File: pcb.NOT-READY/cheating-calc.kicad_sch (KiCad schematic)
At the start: 22 parts, among them J1 Conn_01x04, J2 Conn_01x04, Q1 MMBF170, Q2 MMBF170, U1 ESP32-C3-MINI-1-N4, U2 AP7215-33YG-13, U3 TLV75533PDQNR, U4 TLV75533PDRVR

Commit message: update cap
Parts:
- removed C1, C2: CL21B105KBFNNNE, easyeda2kicad:C0805, symbol easyeda2kicad:CL21B105KBFNNNE
- added C1, C2: CL21B105KPFNNNE, easyeda2kicad:C0805, symbol easyeda2kicad:CL21B105KPFNNNE
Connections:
- net +3.3V: now also C2.1
- net +5V: now also C1.1
- net GND: now also C1.2, C2.2
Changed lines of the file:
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@@
-	)
-	(symbol
-		(lib_id "easyeda2kicad:CL21B105KBFNNNE")
-		(at 100.33 74.93 270)
-		(unit 1)
-		(exclude_from_sim no)
-		(in_bom yes)
-		(on_board yes)
-		(dnp no)
-		(property "Reference" "C1"
-			(at 96.774 74.93 0)
-			(effects
-				(font
-					(size 1.27 1.27)
-				)
-			)
-		)
-		(property "Value" "CL21B105KBFNNNE"
-			(at 104.14 74.93 0)
-			(effects
-				(font
-					(size 1.27 1.27)
-				)
-			)
-		)
-		(property "Footprint" "easyeda2kicad:C0805"
-			(at 92.71 74.93 0)
-			(effects
-				(font
-					(size 1.27 1.27)
-				)
-				(hide yes)
-			)
-		)
-		(property "Datasheet" "https://lcsc.com/product-detail/Multilayer-Ceramic-Capacitors-MLCC-SMD-SMT_SAMSUNG_CL21B105KBFNNNE_1uF-105-10-50V_C28323.html"
-			(at 90.17 74.93 0)
-			(effects
-				(font
-					(size 1.27 1.27)
-				)
-				(hide yes)
-			)
-		)
-		(property "Description" ""
-			(at 100.33 74.93 0)
-			(effects
-				(font
-					(size 1.27 1.27)
-				)
-				(hide yes)
-			)
-		)
-		(property "LCSC Part" "C28323"
-			(at 87.63 74.93 0)
-			(effects
-				(font
-					(size 1.27 1.27)
-				)
-				(hide yes)
-			)
-		)
-		(pin "2"
-		)
-		(pin "1"
-		)
-		(instances
-			(project "cheating-calc"
-				(path "/dc32c202-8f02-44ca-a16c-c11d7f3acb8d"
-					(reference "C1")
-					(unit 1)
-				)
-			)
-		)
 	)
 	(symbol
@@
 	)
 	(symbol
+		(lib_id "easyeda2kicad:CL21B105KPFNNNE")
+		(at 128.27 74.93 270)
+		(unit 1)
+		(exclude_from_sim no)
+		(in_bom yes)
+		(on_board yes)
+		(dnp no)
+		(property "Reference" "C2"
+			(at 123.19 74.93 90)
+			(effects
+				(font
+					(size 1.27 1.27)
+				)
+				(justify left)
+			)
+		)
+		(property "Value" "CL21B105KPFNNNE"
+			(at 130.302 74.93 90)
+			(effects
+				(font
+					(size 1.27 1.27)
+				)
+				(justify left)
+			)
+		)
+		(property "Footprint" "easyeda2kicad:C0805"
+			(at 120.65 74.93 0)
+			(effects
+				(font
+					(size 1.27 1.27)
+				)
+				(hide yes)
+			)
+		)
+		(property "Datasheet" "https://lcsc.com/product-detail/Multilayer-Ceramic-Capacitors-MLCC-SMD-SMT_SAMSUNG_CL21B105KPFNNNE_1uF-105-10-10V_C107367.html"
+			(at 118.11 74.93 0)
+			(effects
+				(font
+					(size 1.27 1.27)
+				)
+				(hide yes)
+			)
+		)
+		(property "Description" ""
+			(at 128.27 74.93 0)
+			(effects
+				(font
+					(size 1.27 1.27)
+				)
+				(hide yes)
+			)
+		)
+		(property "LCSC Part" "C107367"
+			(at 115.57 74.93 0)
+			(effects
+				(font
+					(size 1.27 1.27)
+				)
+				(hide yes)
+			)
+		)
+		(pin "1"
+		)
+		(pin "2"
+		)
+		(instances
+			(project "cheating-calc"
+				(path "/dc32c202-8f02-44ca-a16c-c11d7f3acb8d"
+					(reference "C2")
+					(unit 1)
+				)
+			)
+		)
+	)
+	(symbol
 		(lib_id "easyeda2kicad:0603WAF1002T5E")
 		(at 177.8 71.12 0)
@@
 	)
 	(symbol
+		(lib_id "easyeda2kicad:CL21B105KPFNNNE")
+		(at 100.33 74.93 90)
+		(mirror x)
+		(unit 1)
+		(exclude_from_sim no)
+		(in_bom yes)
+		(on_board yes)
+		(dnp no)
+		(property "Reference" "C1"
+			(at 105.41 74.93 90)
+			(effects
+				(font
+					(size 1.27 1.27)
+				)
+				(justify left)
+			)
+		)
+		(property "Value" "CL21B105KPFNNNE"
+			(at 98.298 74.93 90)
+			(effects
+				(font
+					(size 1.27 1.27)
+				)
+				(justify left)
+			)
+		)
+		(property "Footprint" "easyeda2kicad:C0805"
+			(at 107.95 74.93 0)
+			(effects
+				(font
+					(size 1.27 1.27)
+				)
+				(hide yes)
+			)
+		)
+		(property "Datasheet" "https://lcsc.com/product-detail/Multilayer-Ceramic-Capacitors-MLCC-SMD-SMT_SAMSUNG_CL21B105KPFNNNE_1uF-105-10-10V_C107367.html"
+			(at 110.49 74.93 0)
+			(effects
+				(font
+					(size 1.27 1.27)
+				)
+				(hide yes)
+			)
+		)
+		(property "Description" ""
+			(at 100.33 74.93 0)
+			(effects
+				(font
+					(size 1.27 1.27)
+				)
+				(hide yes)
+			)
+		)
+		(property "LCSC Part" "C107367"
+			(at 113.03 74.93 0)
+			(effects
+				(font
+					(size 1.27 1.27)
+				)
+				(hide yes)
+			)
+		)
+		(pin "1"
+		)
+		(pin "2"
+		)
+		(instances
+			(project ""
+				(path "/dc32c202-8f02-44ca-a16c-c11d7f3acb8d"
+					(reference "C1")
+					(unit 1)
+				)
+			)
+		)
+	)
+	(symbol
 		(lib_id "Jumper:SolderJumper_2_Open")
 		(at 166.37 68.58 0)
@@
 					(unit 1)
 				)
-			)
-		)
-	)
-	(symbol
-		(lib_id "easyeda2kicad:CL21B105KBFNNNE")
-		(at 128.27 74.93 270)
-		(unit 1)
-		(exclude_from_sim no)
-		(in_bom yes)
-		(on_board yes)
-		(dnp no)
-		(property "Reference" "C2"
-			(at 124.714 74.93 0)
-			(effects
-				(font
-					(size 1.27 1.27)
-				)
-			)
-		)
-		(property "Value" "CL21B105KBFNNNE"
-			(at 132.08 74.93 0)
-			(effects
-				(font
-					(size 1.27 1.27)
-				)
-			)
-		)
-		(property "Footprint" "easyeda2kicad:C0805"
-			(at 120.65 74.93 0)
-			(effects
-				(font
-					(size 1.27 1.27)
-				)
-				(hide yes)
-			)
-		)
-		(property "Datasheet" "https://lcsc.com/product-detail/Multilayer-Ceramic-Capacitors-MLCC-SMD-SMT_SAMSUNG_CL21B105KBFNNNE_1uF-105-10-50V_C28323.html"
-			(at 118.11 74.93 0)
-			(effects
-				(font
-					(size 1.27 1.27)
-				)
-				(hide yes)
-			)
-		)
-		(property "Description" ""
-			(at 128.27 74.93 0)
-			(effects
-				(font
-					(size 1.27 1.27)
-				)
-				(hide yes)
-			)
-		)
-		(property "LCSC Part" "C28323"
-			(at 115.57 74.93 0)
-			(effects
-				(font
-					(size 1.27 1.27)
-				)
-				(hide yes)
-			)
-		)
-		(pin "2"
-		)
-		(pin "1"
-		)
-		(instances
-			(project "cheating-calc"
-				(path "/dc32c202-8f02-44ca-a16c-c11d7f3acb8d"
-					(reference "C2")
-					(unit 1)
-				)

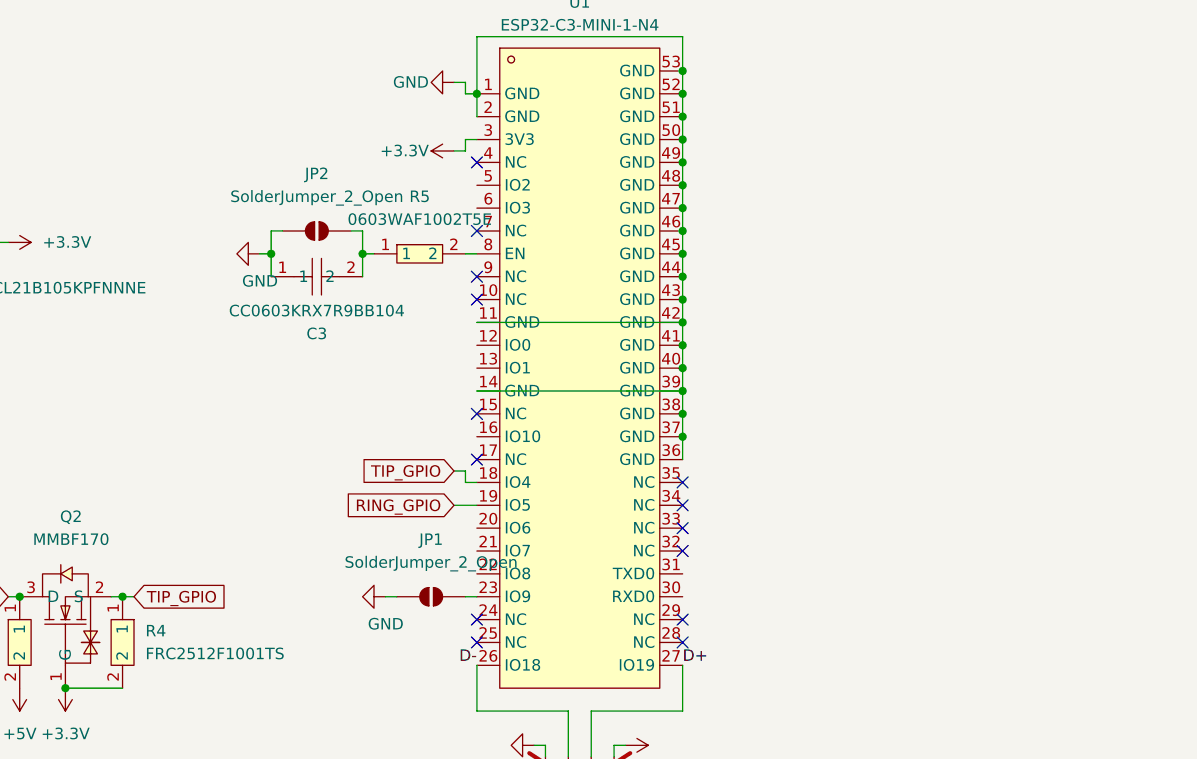
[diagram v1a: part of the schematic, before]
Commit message: Update PCB to add programming pins
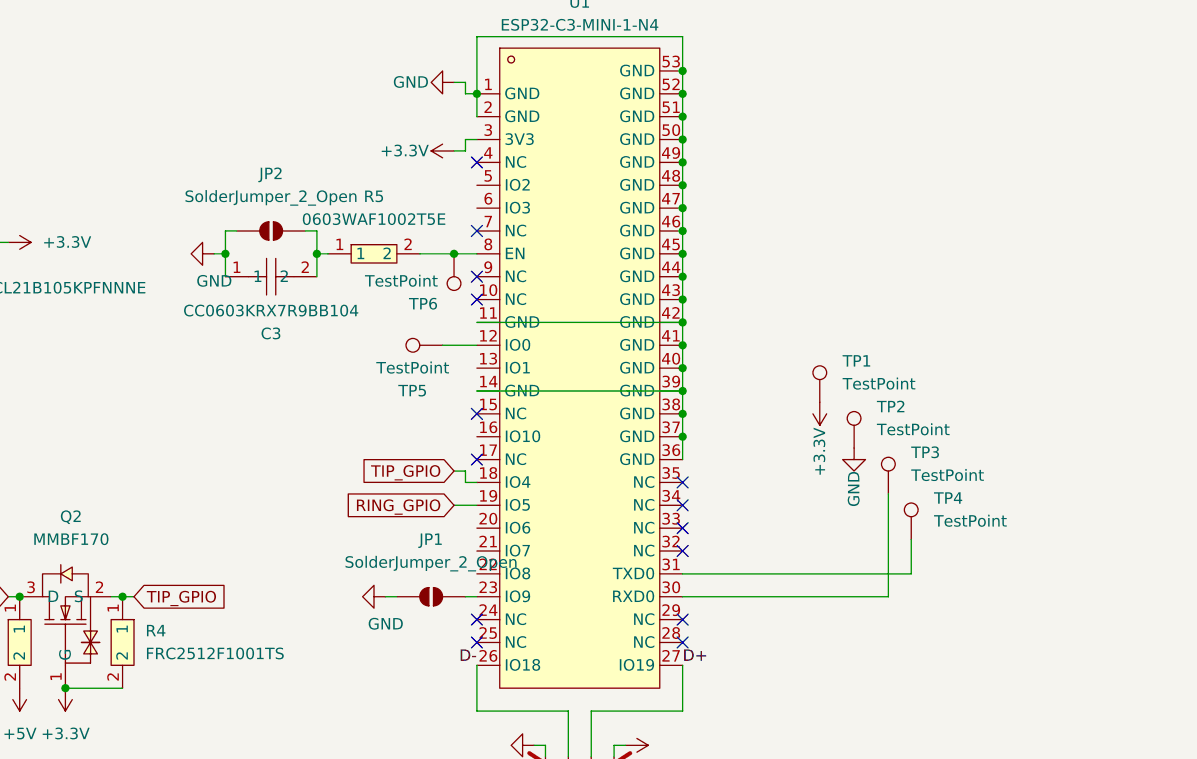
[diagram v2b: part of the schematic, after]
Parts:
- added TP1, TP2, TP3, TP4, TP5, TP6: TestPoint, TestPoint:TestPoint_Pad_D1.0mm, symbol Connector:TestPoint
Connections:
- net +3.3V: now also TP1.1
- net GND: now also TP2.1
- net at R5.2, U1.8 (EN): now also TP6.1
- net at U1.12 (IO0): now also TP5.1
- net at U1.30 (RXD0): now also TP3.1
- net at U1.31 (TXD0): now also TP4.1
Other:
- moved on the sheet: C3, JP2, R5

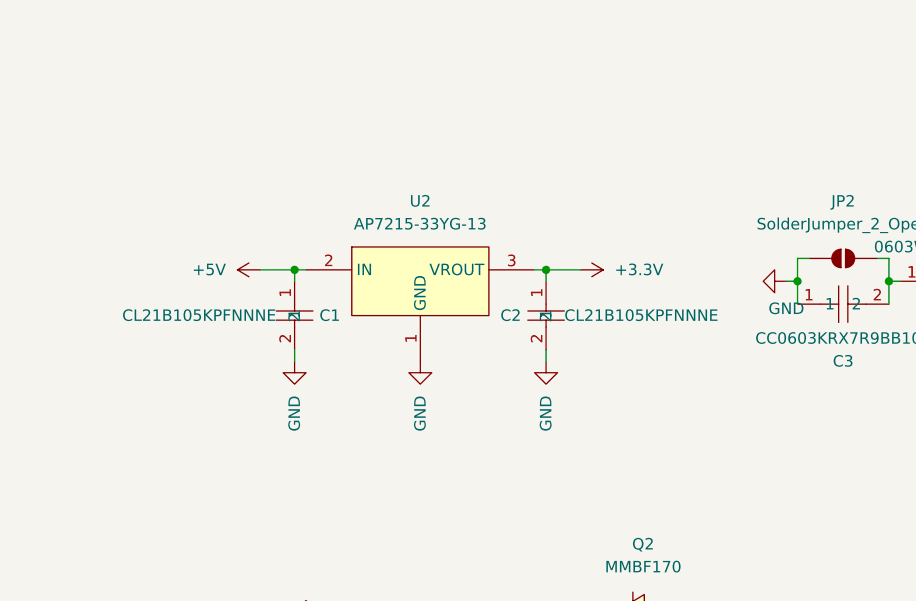
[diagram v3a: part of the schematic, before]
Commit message: update to use a cheaper more avalible LDO
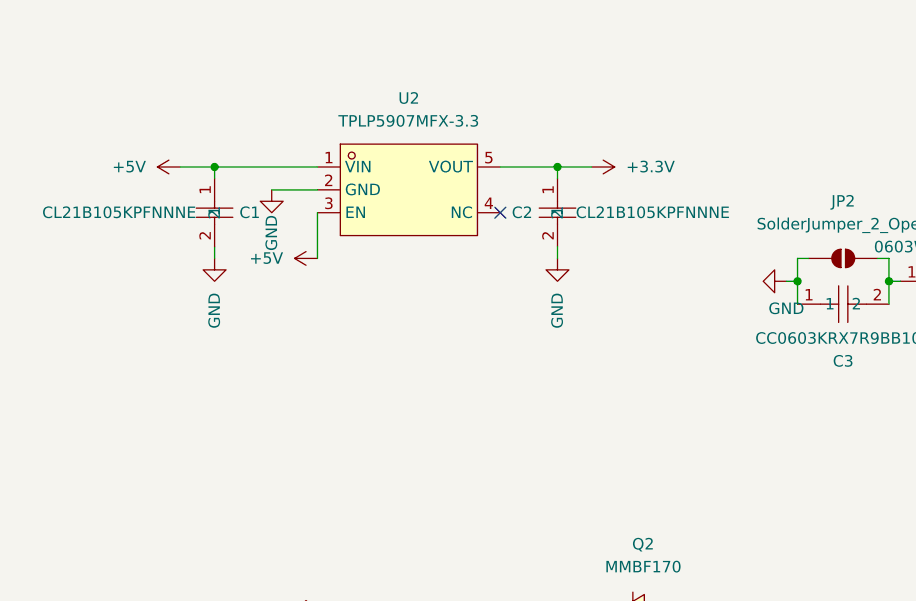
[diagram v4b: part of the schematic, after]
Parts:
- removed U2: AP7215-33YG-13, easyeda2kicad:SOT-89-3_L4.5-W2.5-P1.50-LS4.2-BR, symbol easyeda2kicad:AP7215-33YG-13
- added U2: TPLP5907MFX-3.3, easyeda2kicad:SOT-23-5_L2.9-W1.6-P0.95-LS2.8-BR, symbol easyeda2kicad:TPLP5907MFX-3.3
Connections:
- net +3.3V: now also U2.5 (VOUT)
- net +5V: now also U2.1 (VIN), U2.3 (EN)
- net GND: now also U2.2 (GND)
- no-connect marks 18 -> 19
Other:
- moved on the sheet: C1, C2

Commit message: update and add tht version
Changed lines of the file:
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@@
 (kicad_sch
-	(version 20231120)
+	(version 20250114)
 	(generator "eeschema")
-	(generator_version "8.0")
+	(generator_version "9.0")
 	(paper "A4")
 	(junction
@@
 	(label "D+"
 		(at 207.01 116.84 0)
-		(fields_autoplaced yes)
 		(effects
 			(font
@@
 	(label "D-"
 		(at 184.15 116.84 180)
-		(fields_autoplaced yes)
 		(effects
 			(font
@@
 		)
 	)
+	(embedded_fonts no)
 )
